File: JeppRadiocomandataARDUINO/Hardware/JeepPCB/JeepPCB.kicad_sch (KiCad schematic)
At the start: 2 parts, among them J1 Conn_01x03_Male

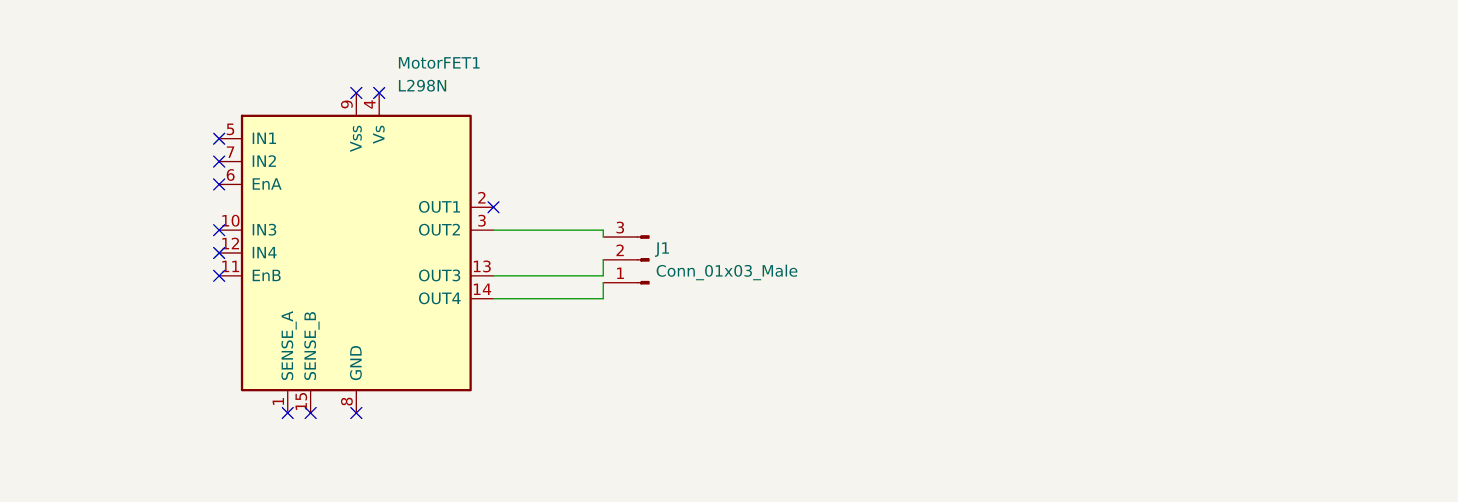
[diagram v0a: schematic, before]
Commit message: Creazione del PCB personalizzato
Design in KiCad e rimozione delle componenti necessarie
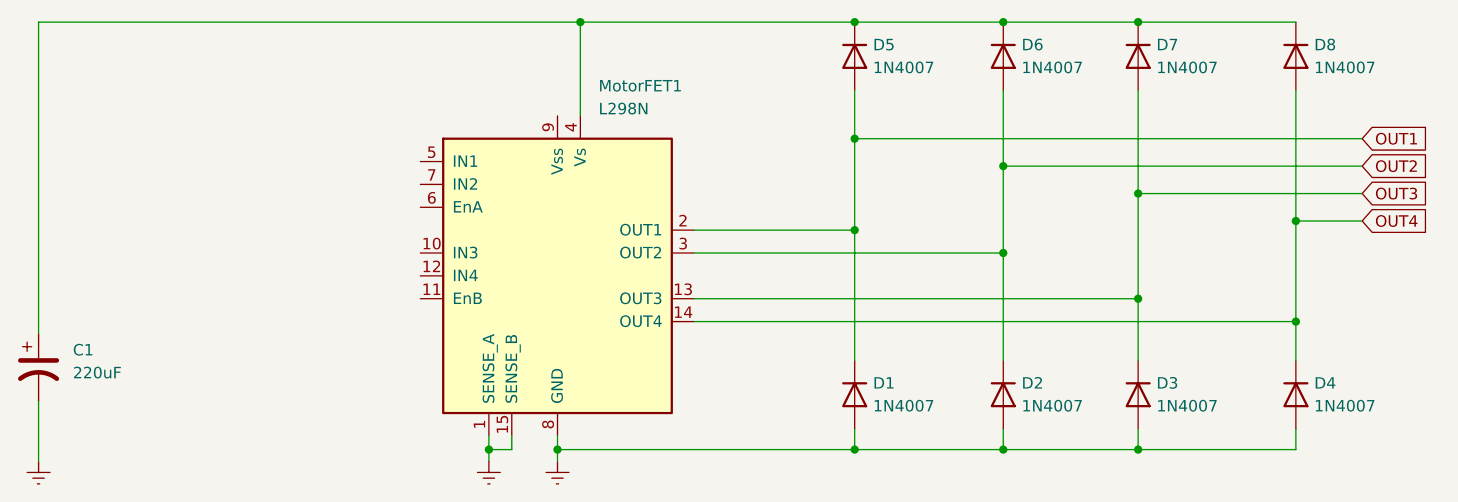
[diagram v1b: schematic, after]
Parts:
- removed J1: Conn_01x03_Male, Connector_PinHeader_1.00mm:PinHeader_1x03_P1.00mm_Vertical, symbol Connector:Conn_01x03_Male
- added C1: 220uF, Capacitor_SMD:C_Elec_4x5.8, symbol Device:C_Polarized_US
- added D1, D2, D3, D4, D5, D6, D7, D8: 1N4007, Diode_THT:D_DO-41_SOD81_P10.16mm_Horizontal, symbol Diode:1N4007
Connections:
- net Earth: now reaches MotorFET1.1 (SENSE_A)
- net Earth: now also MotorFET1.15 (SENSE_B), MotorFET1.8 (GND), C1.2, D1.2 (A), D2.2 (A), D3.2 (A), D4.2 (A)
- net OUT3: now reaches MotorFET1.13 (OUT3)
- net OUT3: now also D3.1 (K), D7.2 (A)
- net OUT4: now reaches MotorFET1.14 (OUT4)
- net OUT4: now also D4.1 (K), D8.2 (A)
- net OUT1: now reaches MotorFET1.2 (OUT1)
- net OUT1: now also D1.1 (K), D5.2 (A)
- net OUT2: now reaches MotorFET1.3 (OUT2)
- net OUT2: now also D2.1 (K), D6.2 (A)
- net at MotorFET1.4 (Vs): now also C1.1, D5.1 (K), D6.1 (K), D7.1 (K), D8.1 (K)
- no-connect marks 12 -> 0
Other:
- moved on the sheet: MotorFET1
